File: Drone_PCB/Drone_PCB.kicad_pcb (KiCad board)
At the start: 2 copper layers, 59 parts, among them J1 Conn_01x04_Pin, J2 Conn_01x08_Socket, J3 Conn_01x05_Socket, J4 Conn_01x02_Socket, J5 Conn_01x02_Socket, J6 Conn_01x02_Socket, J7 Conn_01x02_Socket, J8 Conn_01x02_Socket, J9 USB_B_Micro, Q1 AO3400A, Q2 AO3400A, Q3 AO3400A, Q4 AO3400A, Q5 AO3400A, Q6 AO3400A, SW1 SW_Push, SW2 SW_SPST, U1 STM32F411RCT6, U2 AP2112K-3.3, U3 TP4056-42-ESOP8, U4 DW01A, Y1 26MHz

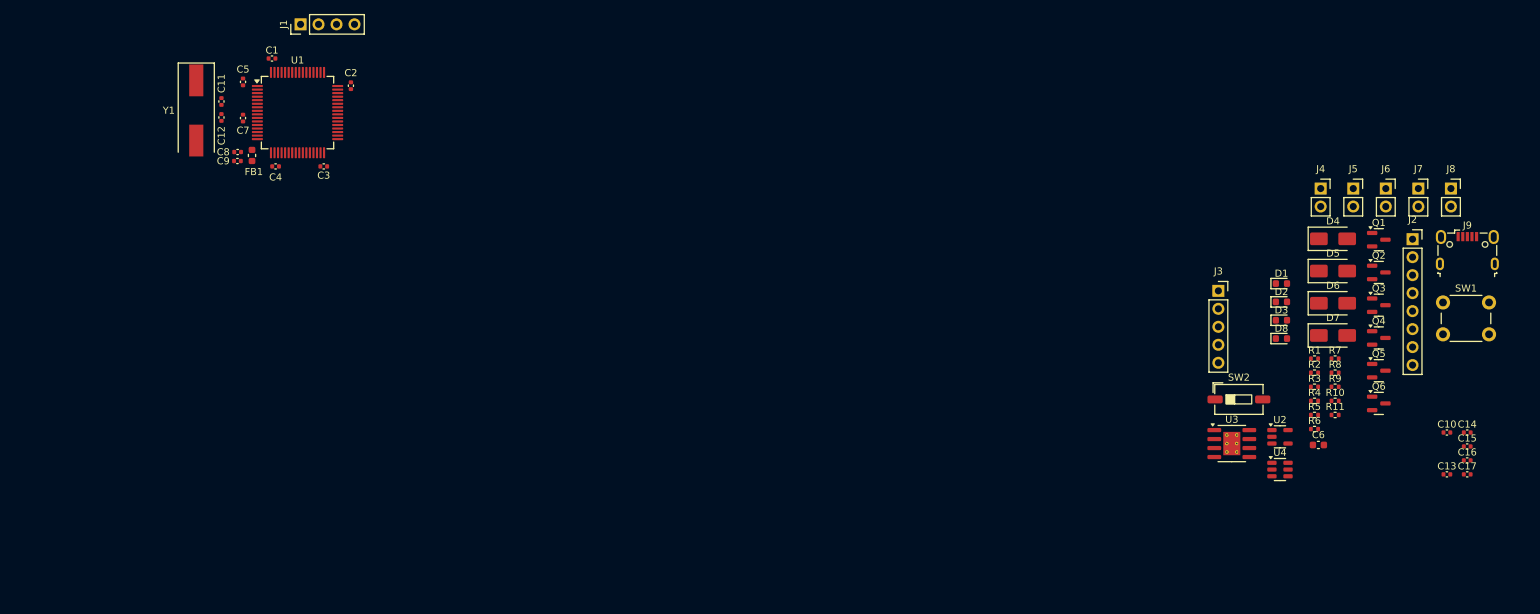
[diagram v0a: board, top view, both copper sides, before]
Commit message: Arranged I2C, UART and SWD
It looks okay
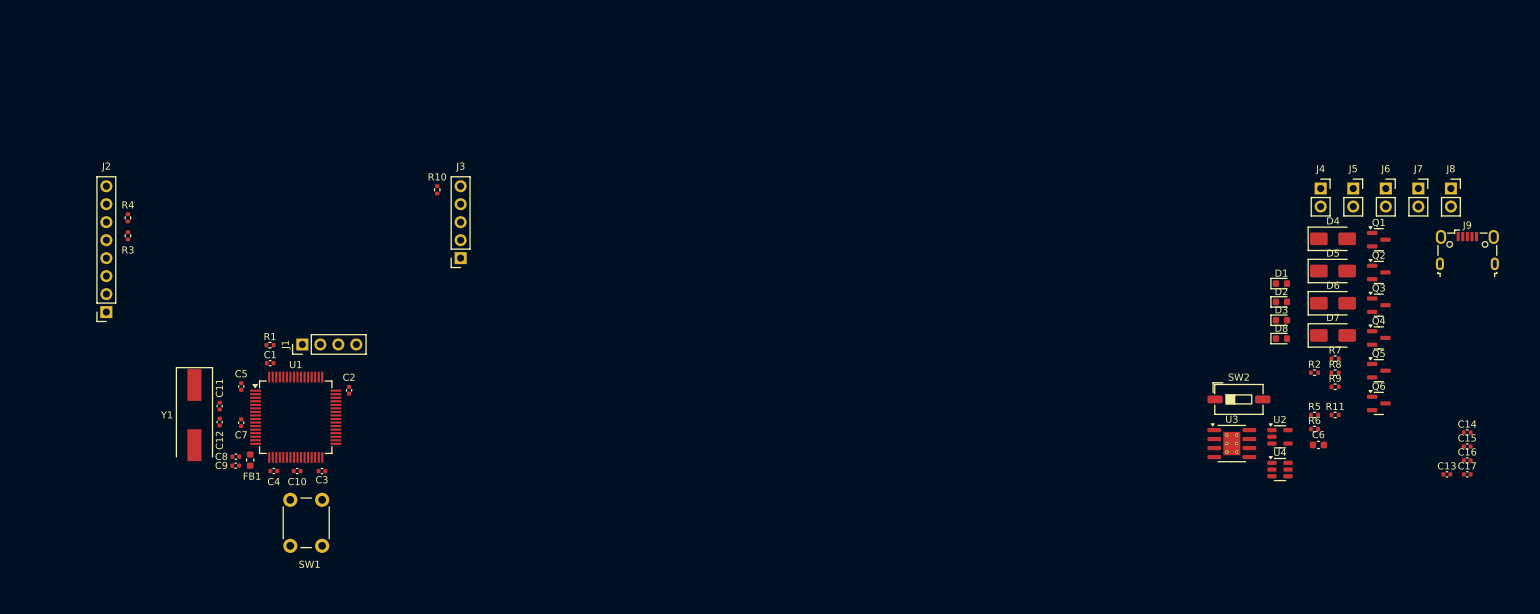
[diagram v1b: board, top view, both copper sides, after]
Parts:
- moved J2 184.8 mm to (47.5, 74.7), turned to 180 degrees
- moved R4 169.6 mm to (50.5, 61.4), turned to 90 degrees
- moved R3 169.0 mm to (50.5, 63.9), turned to -90 degrees
- moved SW1 166.4 mm to (73.5, 107.7), turned to 90 degrees
- moved C10 162.5 mm to (74.5, 97.1)
- moved R1 147.6 mm to (70.6, 79.4)
- moved R10 130.3 mm to (94.2, 57.4), turned to -90 degrees
- moved J3 107.1 mm to (97.5, 67.1), turned to 180 degrees
- moved J1 45.2 mm to (75.2, 79.2)
- moved C3 43.0 mm to (78.0, 97.1)
- moved C4 43.0 mm to (71.1, 97.1)
- moved C7 43.0 mm to (66.5, 90.3)
- moved C12 43.0 mm to (63.5, 90.2)
- moved C2 43.0 mm to (81.8, 85.7)
- moved C5 43.0 mm to (66.5, 85.2)
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
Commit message: PCB #2
Created charging section
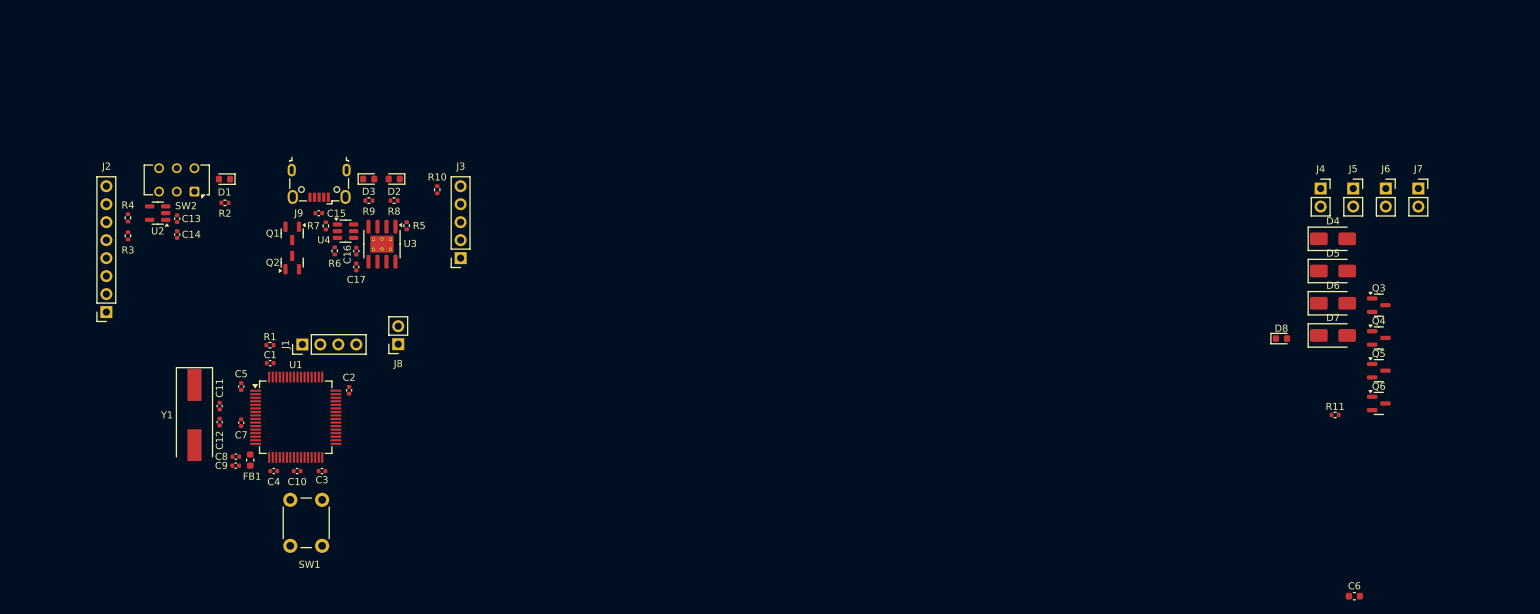
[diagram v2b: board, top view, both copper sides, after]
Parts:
- SW2: footprint Button_Switch_SMD:SW_DIP_SPSTx01_Slide_6.7x4.1mm_W6.73mm_P2.54mm_LowProfile_JPin -> Button_Switch_THT:SW_CK_JS202011AQN_DPDT_Angled
- moved C14 184.4 mm to (57.5, 63.7), turned to 90 degrees
- moved C13 183.0 mm to (57.5, 61.5), turned to 90 degrees
- moved C15 165.5 mm to (77.5, 60.7)
- moved J9 162.5 mm to (77.6, 56.6), turned to 180 degrees
- moved U2 161.6 mm to (54.8, 60.7), turned to 180 degrees
- moved C16 159.7 mm to (82.8, 66.1), turned to -90 degrees
- moved C17 159.6 mm to (82.8, 68.3), turned to 90 degrees
- moved R2 155.8 mm to (64.2, 59.2), turned to 180 degrees
- moved Q2 153.5 mm to (73.8, 67.7), turned to 90 degrees
- moved Q1 153.5 mm to (73.8, 63.6), turned to -90 degrees
- moved SW2 150.4 mm to (59.9, 57.7), turned to 180 degrees
- moved J8 150.3 mm to (88.7, 79.2), turned to 180 degrees
- moved D1 150.0 mm to (64.2, 55.9), turned to 180 degrees
- moved R7 143.8 mm to (78.5, 62.5), turned to 90 degrees
- moved R6 140.7 mm to (79.8, 66.0), turned to -90 degrees
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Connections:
- net Net-(Q1-D) renamed /Q12
- net Net-(Q1-G) renamed /OD
- net Net-(Q2-G) renamed /OC
- net Net-(SW2-B) renamed /PWR
- net Net-(U3-PROG) renamed /PROG
- net Net-(U4-CS) renamed /CS
- net Net-(U4-VCC) renamed /VIN
- C17 pad 1: +3.3V -> /B+
- J8 pad 2: +3.3V -> /B+
- R6 pad 2: +3.3V -> /B+
- SW2 pad 1: +3.3V -> /B+
- U3 pad 5: +3.3V -> /B+

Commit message: PCB #3
Added motors
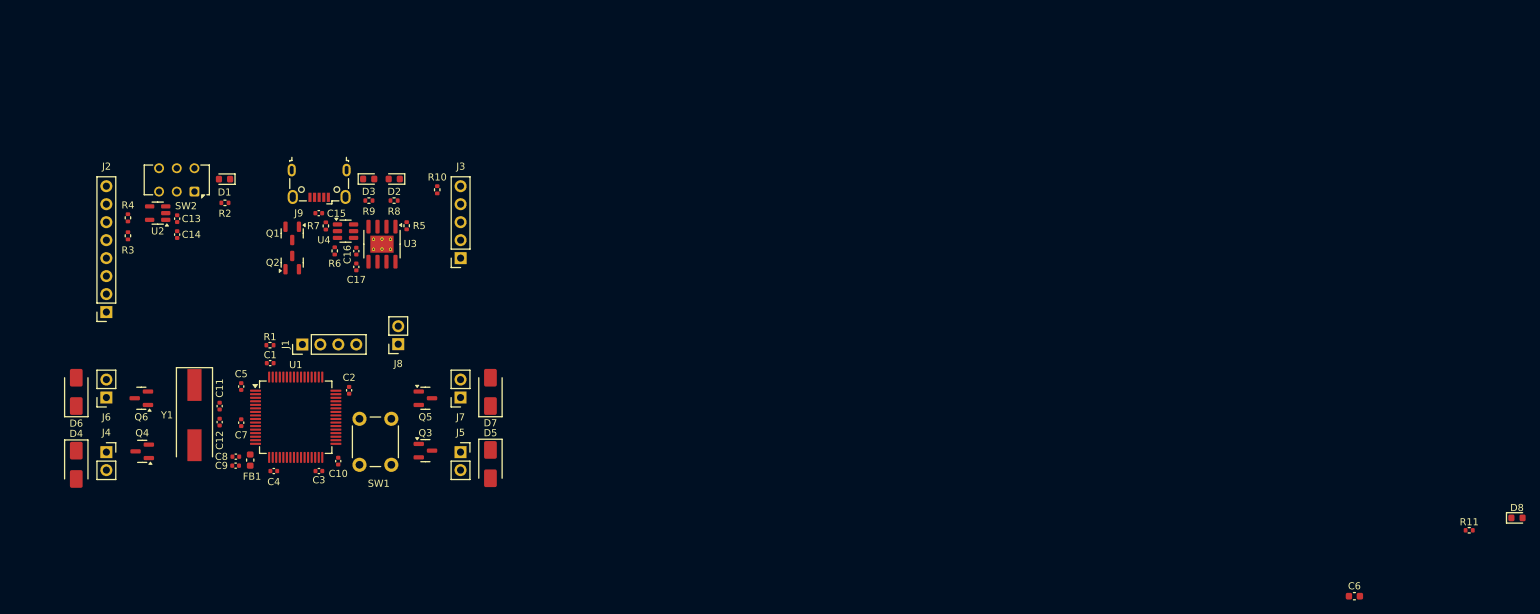
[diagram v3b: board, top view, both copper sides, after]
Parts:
- moved J6 183.1 mm to (47.5, 86.8), turned to 180 degrees
- moved D4 180.4 mm to (43.2, 96.2), turned to -90 degrees
- moved D6 178.0 mm to (43.2, 86.0), turned to 90 degrees
- moved J4 175.5 mm to (47.5, 94.5)
- moved Q4 175.4 mm to (52.6, 94.3), turned to 180 degrees
- moved Q6 174.8 mm to (52.4, 86.8), turned to 180 degrees
- moved J7 138.5 mm to (97.5, 86.8), turned to 180 degrees
- moved Q3 136.2 mm to (92.6, 94.2)
- moved Q5 134.7 mm to (92.6, 86.8)
- moved J5 131.5 mm to (97.5, 94.5)
- moved D5 122.1 mm to (101.8, 96.2), turned to -90 degrees
- moved D7 119.3 mm to (101.8, 86.0), turned to 90 degrees
- moved D8 41.8 mm to (246.8, 103.8)
- moved R11 25.0 mm to (240.0, 105.5)
- moved SW1 15.1 mm to (83.2, 96.2)
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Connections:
- net /MOTOR_LB renamed /PWM_LB
- net /MOTOR_LF renamed /PWM_LF
- net /MOTOR_RB renamed /PWM_RB
- net /MOTOR_RF renamed /PWM_RF
- net Net-(D4-A) renamed /M_LB
- net Net-(D5-A) renamed /M_RB
- net Net-(D6-A) renamed /M_LF
- net Net-(D7-A) renamed /M_RF

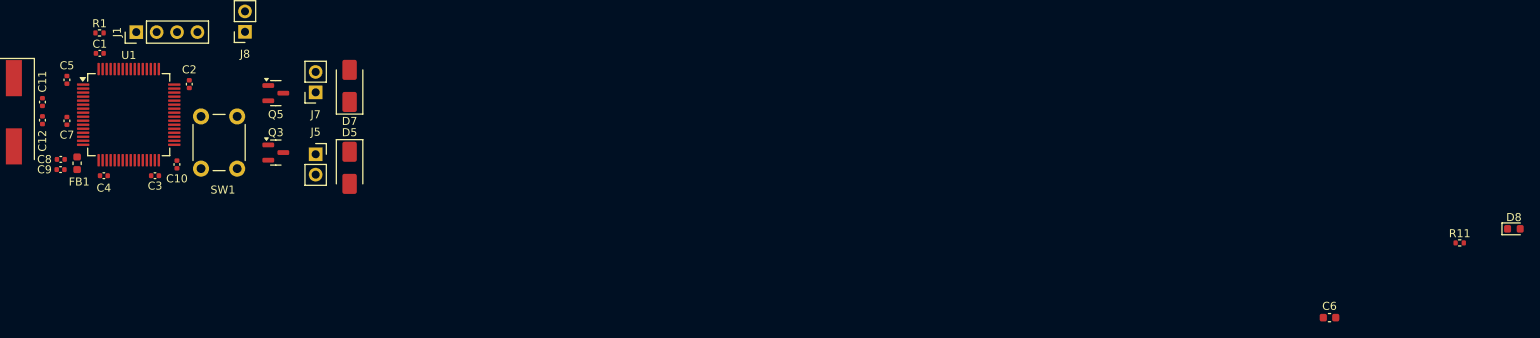
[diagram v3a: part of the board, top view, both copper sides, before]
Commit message: Fast update
PCB didn't save last time
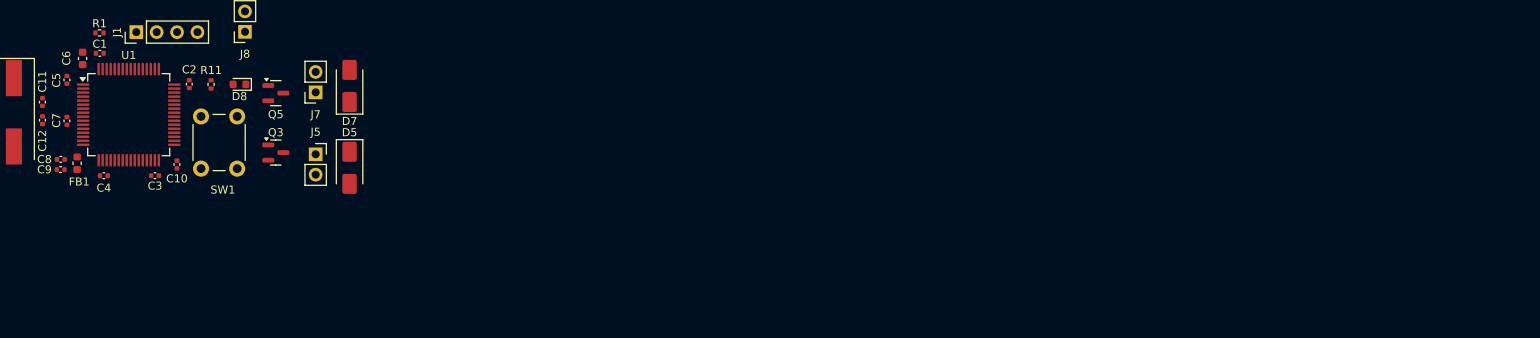
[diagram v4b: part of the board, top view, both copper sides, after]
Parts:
- R11: value 220 -> 1k
- moved D8 159.7 mm to (88.0, 85.8), turned to 180 degrees
- moved C6 158.6 mm to (68.5, 82.5), turned to 90 degrees
- moved R11 156.7 mm to (84.5, 85.8), turned to 90 degrees
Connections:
- net Net-(D8-A) renamed /LED_SIGNAL_VIN

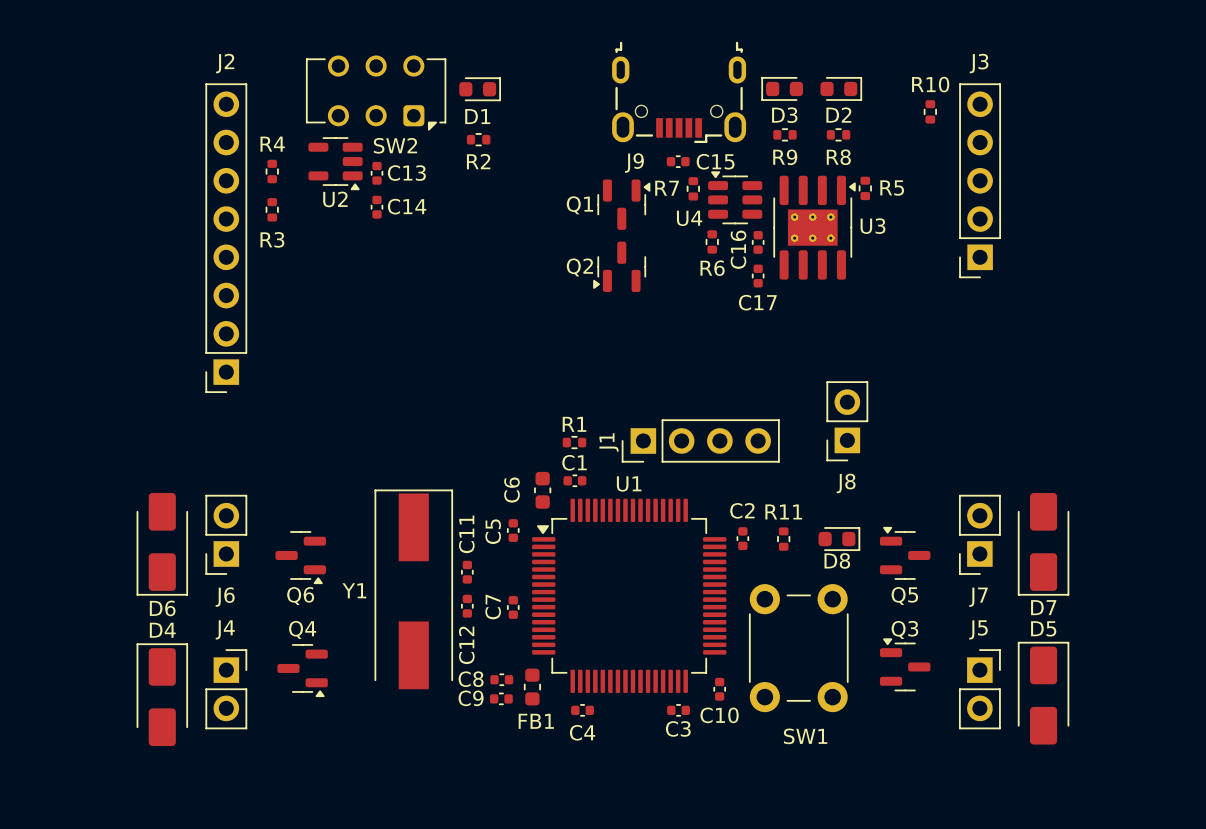
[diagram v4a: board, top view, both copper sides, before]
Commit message: Added Mounting Holers + Edges
Now PCB is almost ready in 3D terms
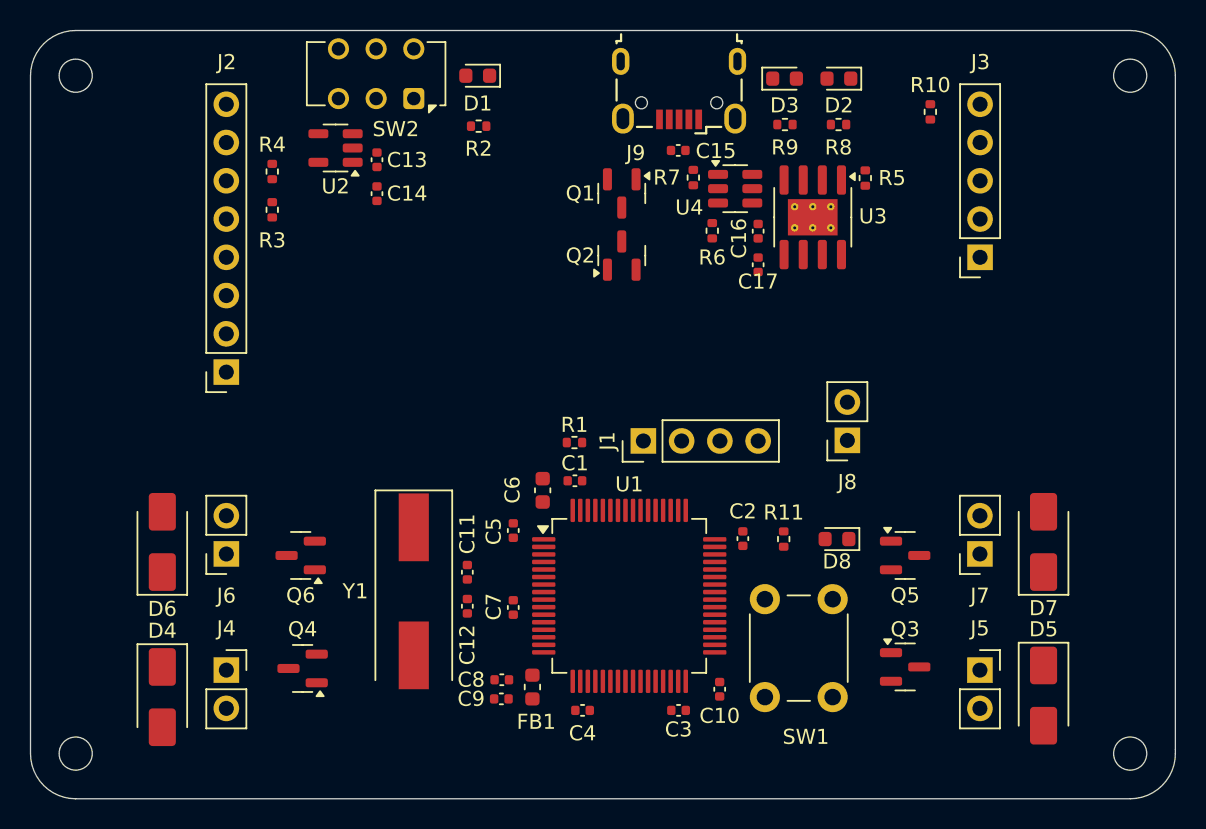
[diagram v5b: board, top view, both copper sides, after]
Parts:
- added H1: MountingHole, MountingHole:MountingHole_2.2mm_M2, F.Cu at (37.5, 55.0)
- added H2: MountingHole, MountingHole:MountingHole_2.2mm_M2, F.Cu at (107.5, 55.0)
- added H3: MountingHole, MountingHole:MountingHole_2.2mm_M2, F.Cu at (37.5, 100.0)
- added H4: MountingHole, MountingHole:MountingHole_2.2mm_M2, F.Cu at (107.5, 100.0)
- moved SW2 1.14 mm to (59.9, 56.5)
- moved U2 0.90 mm to (54.8, 59.8)
- moved C13 0.90 mm to (57.5, 60.6)
- moved C14 0.90 mm to (57.5, 62.8)
- moved D1 0.90 mm to (64.2, 55.0)
- moved R2 0.90 mm to (64.2, 58.4)
- moved C15 0.75 mm to (77.5, 60.0)
- moved Q1 0.75 mm to (73.8, 62.8)
- moved U4 0.75 mm to (81.3, 62.5)
- moved C16 0.75 mm to (82.8, 65.3)
- moved C17 0.75 mm to (82.8, 67.6)
- moved Q2 0.75 mm to (73.8, 66.9)
- moved R6 0.75 mm to (79.8, 65.3)
- moved R7 0.75 mm to (78.5, 61.8)
- moved D2 0.69 mm to (88.2, 55.2)
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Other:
- board outline added: 76 x 51 mm
